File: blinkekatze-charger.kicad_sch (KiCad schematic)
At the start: 28 parts, among them J2 USB_C_Receptacle_USB2.0, Q1 AP90P03Q, U2 CYPD3177

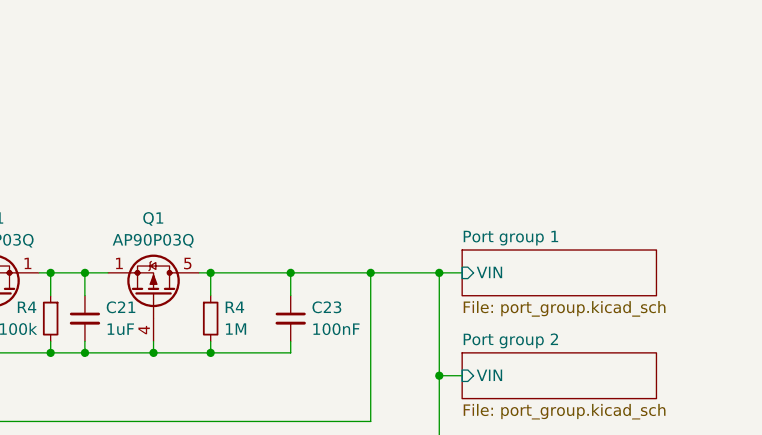
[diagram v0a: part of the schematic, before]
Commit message: Add 5V auxiliary supply
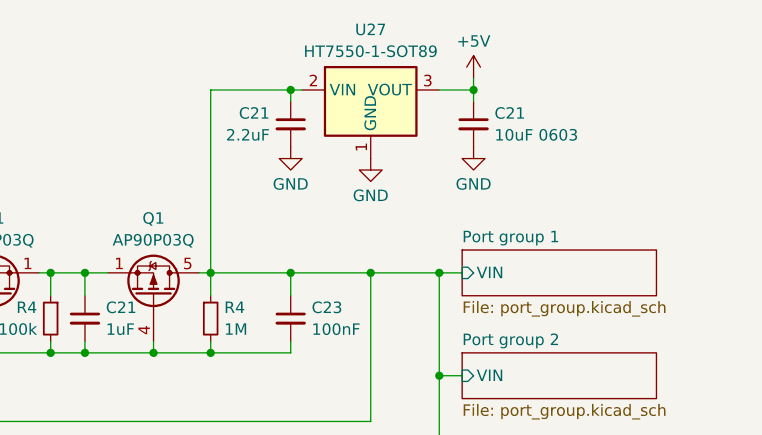
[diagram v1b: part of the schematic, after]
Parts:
- added C21: 10uF 0603, Capacitor_SMD:C_0402_1005Metric, symbol Device:C_Small
- added C21: 2.2uF, Capacitor_SMD:C_0805_2012Metric, symbol Device:C_Small
- added U27: HT7550-1-SOT89, Package_TO_SOT_SMD:SOT-89-3, symbol Regulator_Linear:HT75xx-1-SOT89
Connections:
- net GND: now also C21.2, C21.2, U27.1 (GND)
- net Port group 1/VIN: now also C21.1, U27.2 (VIN)
- new net +5V: C21.1, U27.3 (VOUT)
